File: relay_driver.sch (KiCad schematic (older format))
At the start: 5 parts

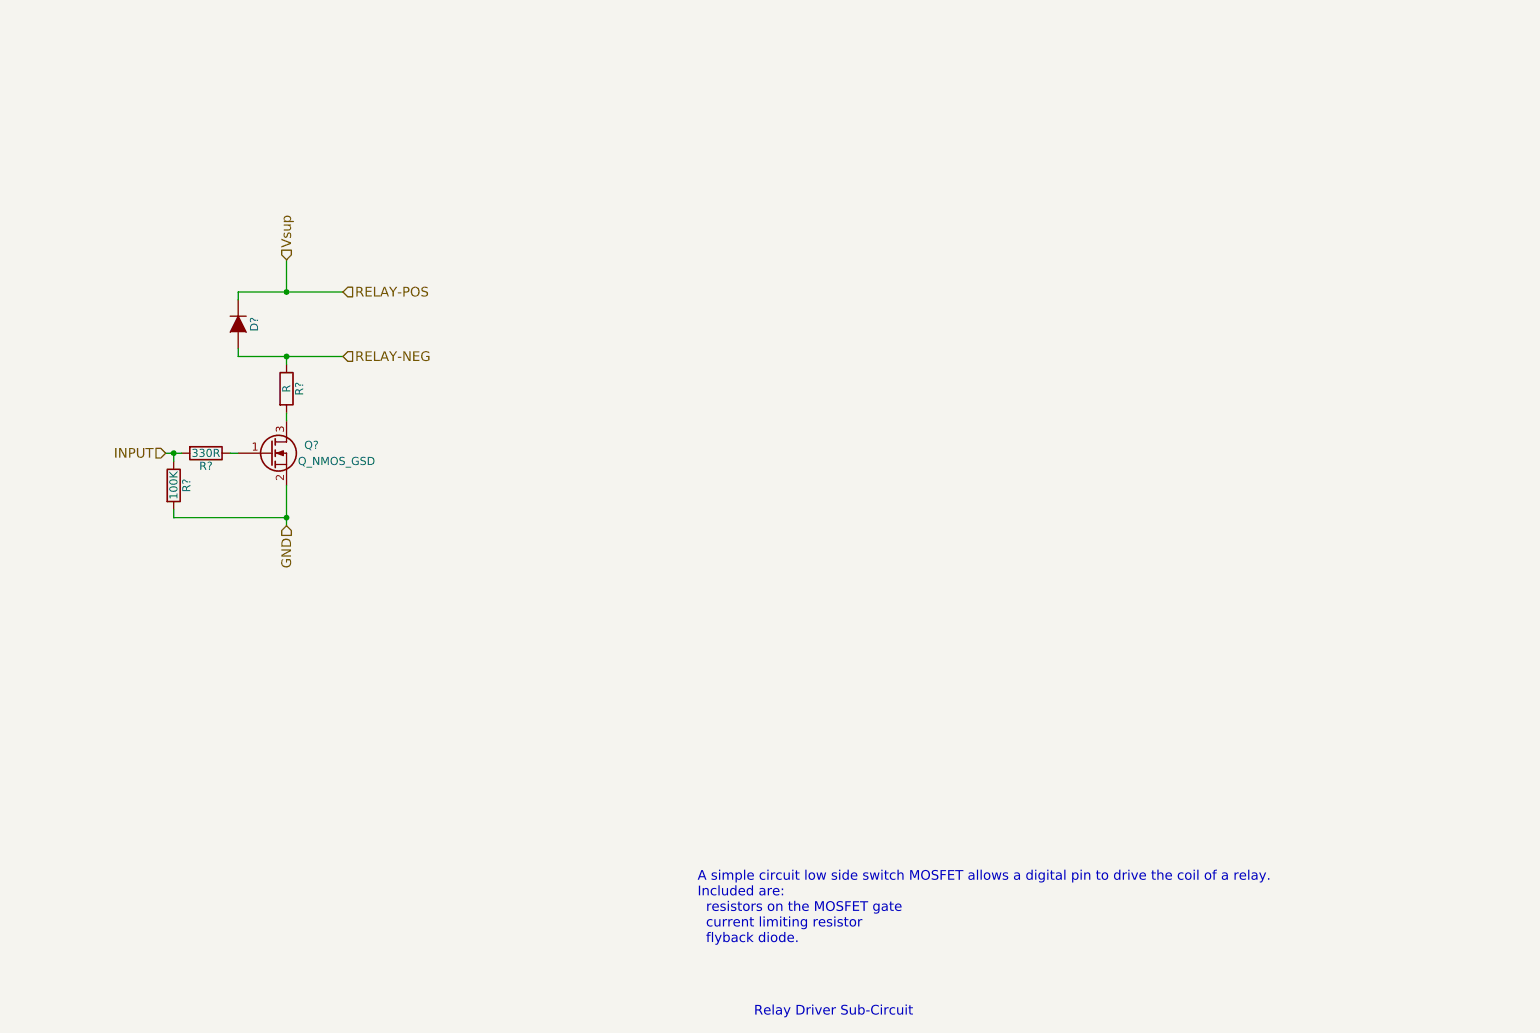
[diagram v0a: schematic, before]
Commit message: added some ICs, started on power, changed sheet sizes
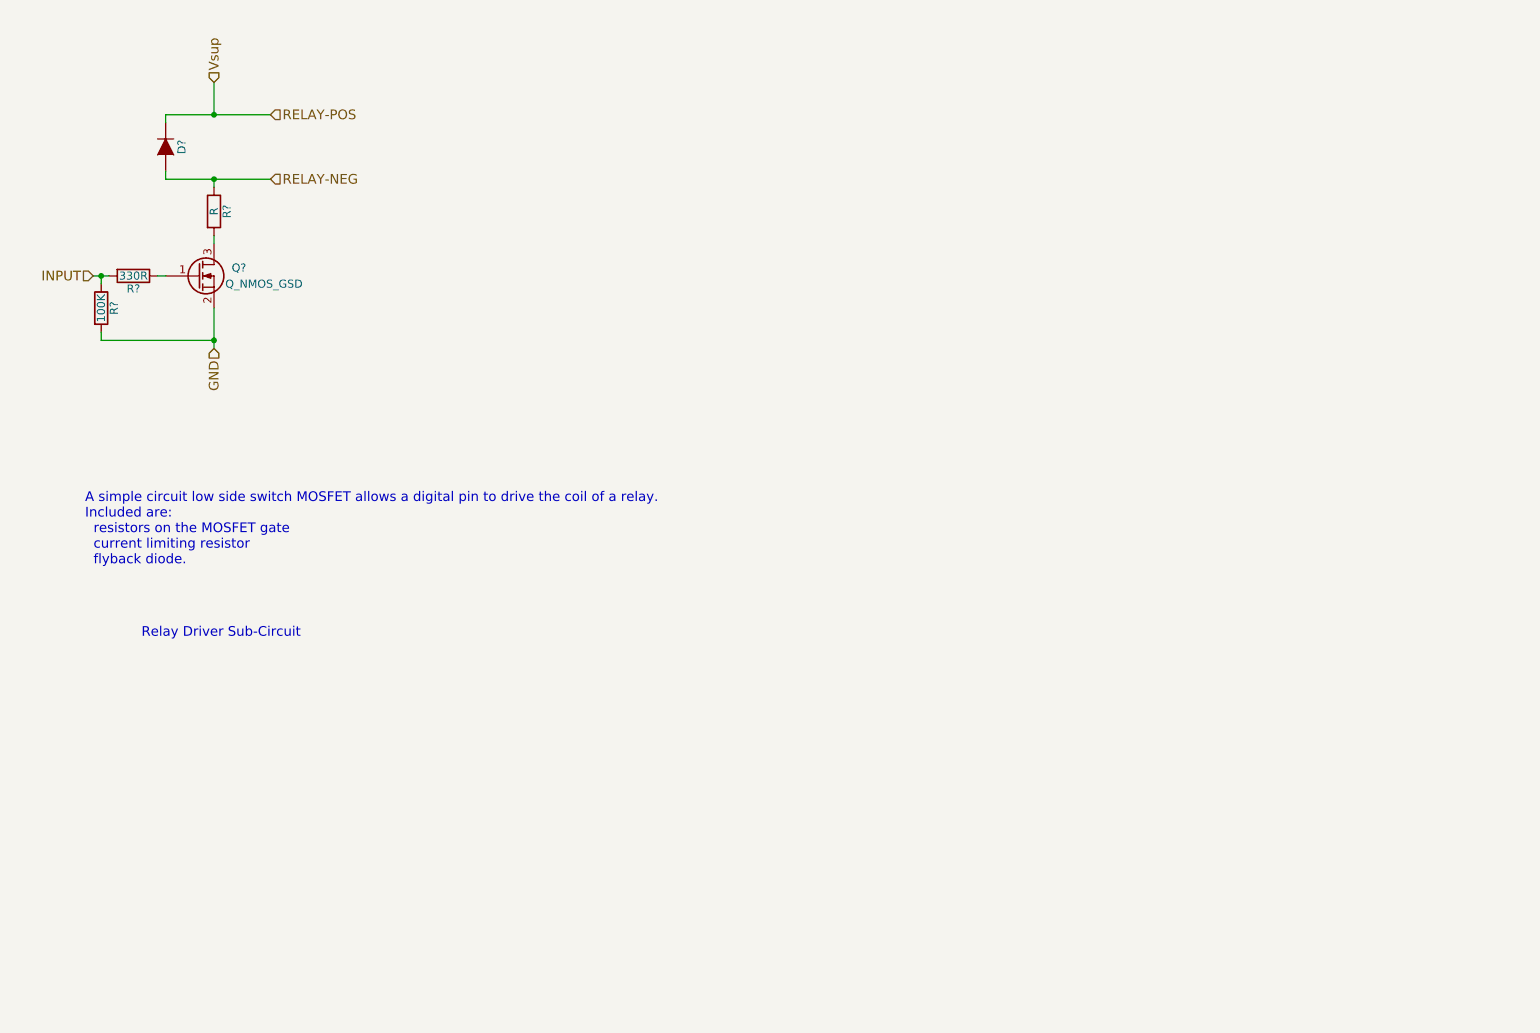
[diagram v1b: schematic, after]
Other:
- moved on the sheet: D?, Q?, R?
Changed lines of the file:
@@
 EELAYER 25 0
 EELAYER END
-$Descr A4 11693 8268
+$Descr User 7874 5906
 encoding utf-8
-Sheet 5 12
+Sheet 2 12
 Title ""
 Date ""
@@
 L Q_NMOS_GSD Q?
 U 1 1 57284B32
-P 4350 4000
+P 3900 2900
 AR Path="/572843F5/57284B32" Ref="Q?"  Part="1"
 AR Path="/5728BD9D/57284B32" Ref="Q?"  Part="1"
-F 0 "Q?" H 4650 4050 50  0000 R CNN
-F 1 "Q_NMOS_GSD" H 5000 3950 50  0000 R CNN
-F 2 "" H 4550 4100 50  0000 C CNN
-F 3 "" H 4350 4000 50  0000 C CNN
-	1    4350 4000
+F 0 "Q?" H 4200 2950 50  0000 R CNN
+F 1 "Q_NMOS_GSD" H 4550 2850 50  0000 R CNN
+F 2 "" H 4100 3000 50  0000 C CNN
+F 3 "" H 3900 2900 50  0000 C CNN
+	1    3900 2900
 	1    0    0    -1
 $EndComp
@@
 L R R?
 U 1 1 57284C7E
-P 3750 4200
+P 3300 3100
 AR Path="/572843F5/57284C7E" Ref="R?"  Part="1"
 AR Path="/5728BD9D/57284C7E" Ref="R?"  Part="1"
-F 0 "R?" V 3830 4200 50  0000 C CNN
-F 1 "100K" V 3750 4200 50  0000 C CNN
-F 2 "" V 3680 4200 50  0000 C CNN
-F 3 "" H 3750 4200 50  0000 C CNN
-	1    3750 4200
+F 0 "R?" V 3380 3100 50  0000 C CNN
+F 1 "100K" V 3300 3100 50  0000 C CNN
+F 2 "" V 3230 3100 50  0000 C CNN
+F 3 "" H 3300 3100 50  0000 C CNN
+	1    3300 3100
 	1    0    0    -1
 $EndComp
@@
 L R R?
 U 1 1 57284CE3
-P 3950 4000
+P 3500 2900
 AR Path="/572843F5/57284CE3" Ref="R?"  Part="1"
 AR Path="/5728BD9D/57284CE3" Ref="R?"  Part="1"
-F 0 "R?" V 4030 4000 50  0000 C CNN
-F 1 "330R" V 3950 4000 50  0000 C CNN
-F 2 "" V 3880 4000 50  0000 C CNN
-F 3 "" H 3950 4000 50  0000 C CNN
-	1    3950 4000
+F 0 "R?" V 3580 2900 50  0000 C CNN
+F 1 "330R" V 3500 2900 50  0000 C CNN
+F 2 "" V 3430 2900 50  0000 C CNN
+F 3 "" H 3500 2900 50  0000 C CNN
+	1    3500 2900
 	0    1    1    0
 $EndComp
@@
 L D D?
 U 1 1 5728508D
-P 4150 3200
+P 3700 2100
 AR Path="/572843F5/5728508D" Ref="D?"  Part="1"
 AR Path="/5728BD9D/5728508D" Ref="D?"  Part="1"
-F 0 "D?" H 4150 3300 50  0000 C CNN
-F 1 "D" H 4150 3100 50  0001 C CNN
-F 2 "" H 4150 3200 50  0000 C CNN
-F 3 "" H 4150 3200 50  0000 C CNN
-	1    4150 3200
+F 0 "D?" H 3700 2200 50  0000 C CNN
+F 1 "D" H 3700 2000 50  0001 C CNN
+F 2 "" H 3700 2100 50  0000 C CNN
+F 3 "" H 3700 2100 50  0000 C CNN
+	1    3700 2100
 	0    1    1    0
 $EndComp
 Wire Wire Line
-	4150 3400 4800 3400
+	3700 2300 4350 2300
 Wire Wire Line
-	4150 3400 4150 3350
-Connection ~ 4450 3400
+	3700 2300 3700 2250
+Connection ~ 4000 2300
 Wire Wire Line
-	4150 3050 4150 3000
+	3700 1950 3700 1900
 $Comp
 L R R?
 U 1 1 5728580D
-P 4450 3600
+P 4000 2500
 AR Path="/572843F5/5728580D" Ref="R?"  Part="1"
 AR Path="/5728BD9D/5728580D" Ref="R?"  Part="1"
-F 0 "R?" V 4530 3600 50  0000 C CNN
-F 1 "R" V 4450 3600 50  0000 C CNN
-F 2 "" V 4380 3600 50  0000 C CNN
-F 3 "" H 4450 3600 50  0000 C CNN
-	1    4450 3600
+F 0 "R?" V 4080 2500 50  0000 C CNN
+F 1 "R" V 4000 2500 50  0000 C CNN
+F 2 "" V 3930 2500 50  0000 C CNN
+F 3 "" H 4000 2500 50  0000 C CNN
+	1    4000 2500
 	1    0    0    -1
 $EndComp
 Wire Wire Line
-	4450 3800 4450 3750
-Text Notes 7350 7500 0    60   ~ 0
+	4000 2700 4000 2650
+Text Notes 3550 5150 0    60   ~ 0
 Relay Driver Sub-Circuit
-Text Notes 7000 7050 0    60   ~ 0
+Text Notes 3200 4700 0    60   ~ 0
 A simple circuit low side switch MOSFET allows a digital pin to drive the coil of a relay.\nIncluded are:\n  resistors on the MOSFET gate\n  current limiting resistor\n  flyback diode.
 Wire Wire Line
-	4450 4200 4450 4450
+	4000 3100 4000 3350
 Wire Wire Line
-	4450 4400 3750 4400
+	4000 3300 3300 3300
 Wire Wire Line
-	3750 4400 3750 4350
+	3300 3300 3300 3250
 Wire Wire Line
-	4100 4000 4150 4000
+	3650 2900 3700 2900
 Wire Wire Line
-	3700 4000 3800 4000
+	3250 2900 3350 2900
 Wire Wire Line
-	3750 4000 3750 4050
+	3300 2900 3300 2950
 Wire Wire Line
-	4450 3450 4450 3400
-Connection ~ 4450 4400
-Text HLabel 4450 4450 3    60   Input ~ 0
+	4000 2350 4000 2300
+Connection ~ 4000 3300
+Text HLabel 4000 3350 3    60   Input ~ 0
 GND
-Connection ~ 3750 4000
-Text HLabel 3700 4000 0    60   Input ~ 0
+Connection ~ 3300 2900
+Text HLabel 3250 2900 0    60   Input ~ 0
 INPUT
-Text HLabel 4450 2800 1    60   Input ~ 0
+Text HLabel 4000 1700 1    60   Input ~ 0
 Vsup
-Text HLabel 4800 3000 2    60   Input ~ 0
+Text HLabel 4350 1900 2    60   Input ~ 0
 RELAY-POS
-Text HLabel 4800 3400 2    60   Input ~ 0
+Text HLabel 4350 2300 2    60   Input ~ 0
 RELAY-NEG
 Wire Wire Line
-	4150 3000 4800 3000
+	3700 1900 4350 1900
 Wire Wire Line
-	4450 2800 4450 3000
-Connection ~ 4450 3000
+	4000 1700 4000 1900
+Connection ~ 4000 1900
 $EndSCHEMATC

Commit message: near done, TODO needs 5V sup from HV, etc
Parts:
- R?: footprint (none) -> Resistors_SMD:R_1206_HandSoldering
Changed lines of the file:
@@
 $Descr User 7874 5906
 encoding utf-8
-Sheet 2 12
+Sheet 4 5
 Title ""
 Date ""
@@
 AR Path="/572843F5/57284B32" Ref="Q?"  Part="1"
 AR Path="/5728BD9D/57284B32" Ref="Q?"  Part="1"
+AR Path="/5728B2EB/57284B32" Ref="Q?"  Part="1"
+AR Path="/5728BD96/57284B32" Ref="Q?"  Part="1"
 F 0 "Q?" H 4200 2950 50  0000 R CNN
 F 1 "Q_NMOS_GSD" H 4550 2850 50  0000 R CNN
@@
 AR Path="/572843F5/57284C7E" Ref="R?"  Part="1"
 AR Path="/5728BD9D/57284C7E" Ref="R?"  Part="1"
+AR Path="/5728B2EB/57284C7E" Ref="R?"  Part="1"
+AR Path="/5728BD96/57284C7E" Ref="R?"  Part="1"
 F 0 "R?" V 3380 3100 50  0000 C CNN
 F 1 "100K" V 3300 3100 50  0000 C CNN
@@
 AR Path="/572843F5/57284CE3" Ref="R?"  Part="1"
 AR Path="/5728BD9D/57284CE3" Ref="R?"  Part="1"
+AR Path="/5728B2EB/57284CE3" Ref="R?"  Part="1"
+AR Path="/5728BD96/57284CE3" Ref="R?"  Part="1"
 F 0 "R?" V 3580 2900 50  0000 C CNN
 F 1 "330R" V 3500 2900 50  0000 C CNN
@@
 AR Path="/572843F5/5728508D" Ref="D?"  Part="1"
 AR Path="/5728BD9D/5728508D" Ref="D?"  Part="1"
+AR Path="/5728B2EB/5728508D" Ref="D?"  Part="1"
+AR Path="/5728BD96/5728508D" Ref="D?"  Part="1"
 F 0 "D?" H 3700 2200 50  0000 C CNN
 F 1 "D" H 3700 2000 50  0001 C CNN
@@
 AR Path="/572843F5/5728580D" Ref="R?"  Part="1"
 AR Path="/5728BD9D/5728580D" Ref="R?"  Part="1"
+AR Path="/5728B2EB/5728580D" Ref="R?"  Part="1"
+AR Path="/5728BD96/5728580D" Ref="R?"  Part="1"
 F 0 "R?" V 4080 2500 50  0000 C CNN
-F 1 "R" V 4000 2500 50  0000 C CNN
-F 2 "" V 3930 2500 50  0000 C CNN
+F 1 "R" V 4000 2500 50  0001 C CNN
+F 2 "Resistors_SMD:R_1206_HandSoldering" V 3930 2500 50  0001 C CNN
 F 3 "" H 4000 2500 50  0000 C CNN
 	1    4000 2500

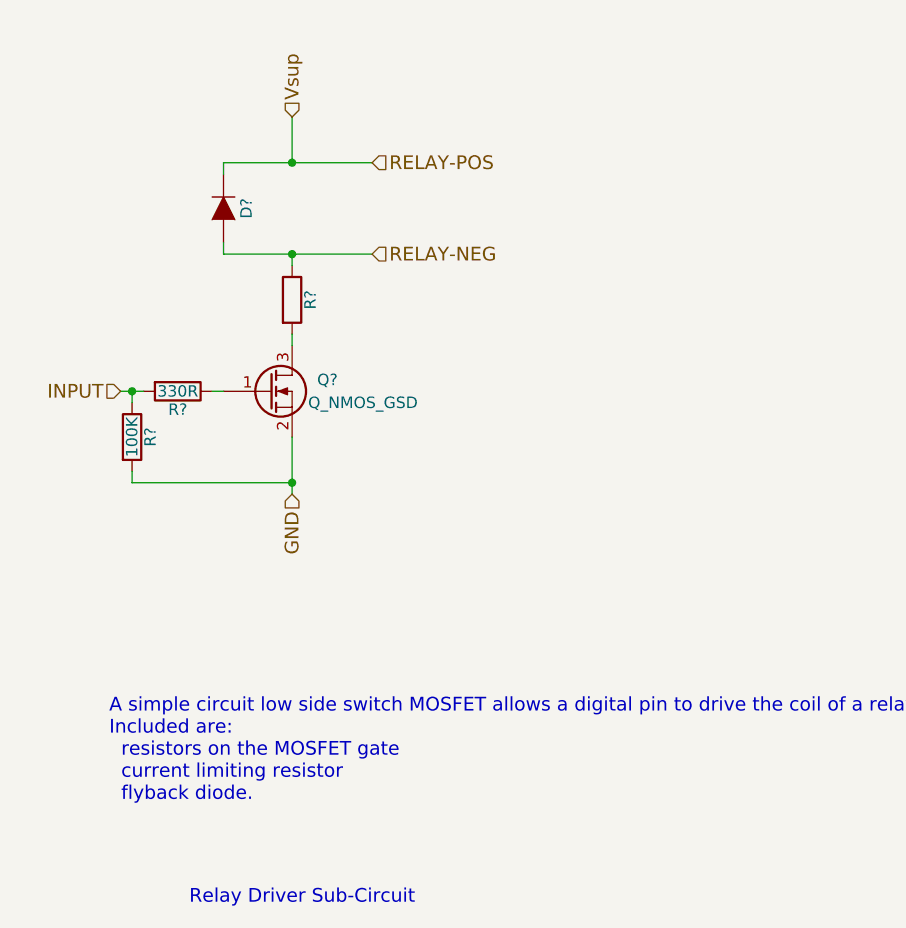
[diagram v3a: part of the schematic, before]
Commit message: WIP but mostly done, needs connector
latch switch changed to using photorelays
added watchdog to relays
added two unidirectional precharge subcircuits
moved ILV relay to onboard
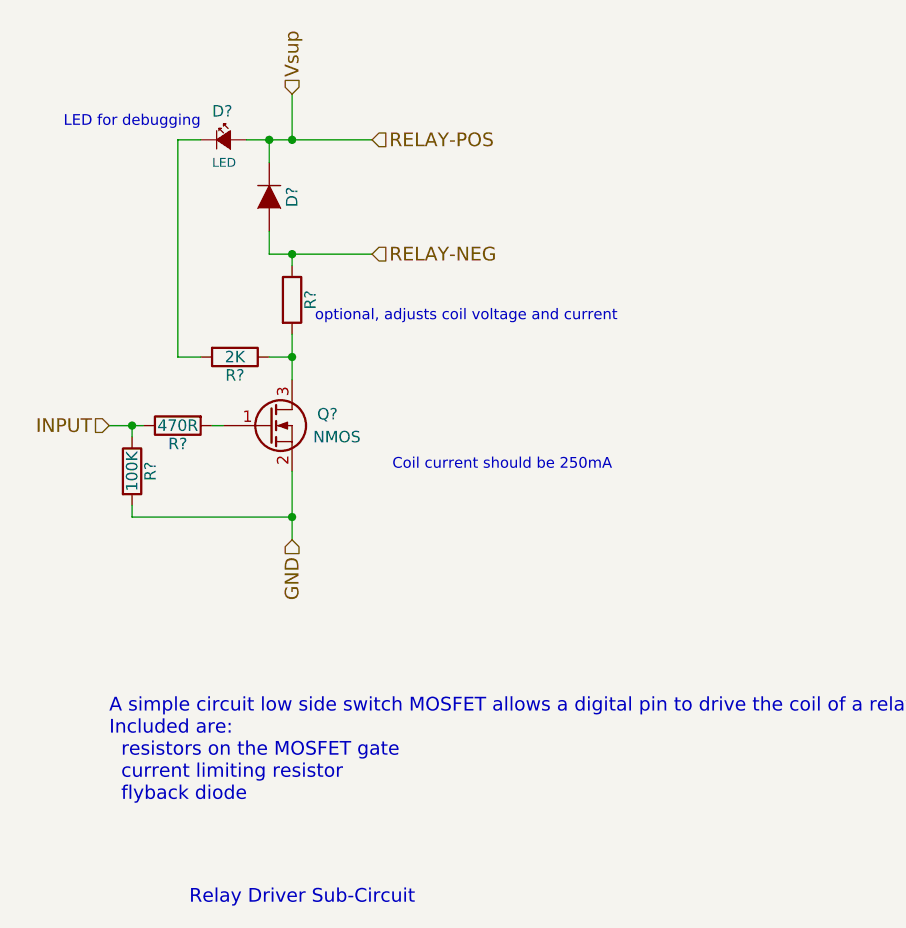
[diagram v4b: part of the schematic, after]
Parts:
- added D?: LED, symbol Led_Small
- added R?: 2K, Resistors_SMD:R_1206_HandSoldering, symbol R
- Q?: value Q_NMOS_GSD -> NMOS
- R?: value 330R -> 470R
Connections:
- net INPUT: now also R?.1; no longer R?.2
- net RELAY-POS: now also D?.2 (A)
- net at Q?.1 (G): now also R?.2; no longer R?.1
- net at Q?.3 (D), R?.2: now also R?.1
- new net: D?.1 (K), R?.2
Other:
- note added: "A simple circuit low side switch MOSFET allows a digital pin to drive the coil of a relay.\nIncluded are:\n resistors on the MOSFET gate\n current limiting resistor\n flyback diode"
- note added: "Coil current should be 250mA"
- note added: "LED for debugging"
- note added: "optional, adjusts coil voltage and current"
- note removed: "A simple circuit low side switch MOSFET allows a digital pin to drive the coil of a relay.\nIncluded are:\n resistors on the MOSFET gate\n current limiting resistor\n flyback diode."
- moved on the sheet: D?, Q?, R?
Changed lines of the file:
@@
 $Descr User 7874 5906
 encoding utf-8
-Sheet 4 7
+Sheet 2 5
 Title ""
 Date ""
@@
 L Q_NMOS_GSD Q?
 U 1 1 57284B32
-P 3900 2900
+P 3900 3050
 AR Path="/572843F5/57284B32" Ref="Q?"  Part="1"
 AR Path="/5728BD9D/57284B32" Ref="Q?"  Part="1"
 AR Path="/5728B2EB/57284B32" Ref="Q?"  Part="1"
 AR Path="/5728BD96/57284B32" Ref="Q?"  Part="1"
-F 0 "Q?" H 4200 2950 50  0000 R CNN
-F 1 "Q_NMOS_GSD" H 4550 2850 50  0000 R CNN
-F 2 "" H 4100 3000 50  0000 C CNN
-F 3 "" H 3900 2900 50  0000 C CNN
-	1    3900 2900
+F 0 "Q?" H 4200 3100 50  0000 R CNN
+F 1 "NMOS" H 4300 3000 50  0000 R CNN
+F 2 "" H 4100 3150 50  0000 C CNN
+F 3 "" H 3900 3050 50  0000 C CNN
+	1    3900 3050
 	1    0    0    -1
 $EndComp
@@
 L R R?
 U 1 1 57284C7E
-P 3300 3100
+P 3300 3250
 AR Path="/572843F5/57284C7E" Ref="R?"  Part="1"
 AR Path="/5728BD9D/57284C7E" Ref="R?"  Part="1"
 AR Path="/5728B2EB/57284C7E" Ref="R?"  Part="1"
 AR Path="/5728BD96/57284C7E" Ref="R?"  Part="1"
-F 0 "R?" V 3380 3100 50  0000 C CNN
-F 1 "100K" V 3300 3100 50  0000 C CNN
-F 2 "" V 3230 3100 50  0000 C CNN
-F 3 "" H 3300 3100 50  0000 C CNN
-	1    3300 3100
+F 0 "R?" V 3380 3250 50  0000 C CNN
+F 1 "100K" V 3300 3250 50  0000 C CNN
+F 2 "" V 3230 3250 50  0000 C CNN
+F 3 "" H 3300 3250 50  0000 C CNN
+	1    3300 3250
 	1    0    0    -1
 $EndComp
@@
 L R R?
 U 1 1 57284CE3
-P 3500 2900
+P 3500 3050
 AR Path="/572843F5/57284CE3" Ref="R?"  Part="1"
 AR Path="/5728BD9D/57284CE3" Ref="R?"  Part="1"
 AR Path="/5728B2EB/57284CE3" Ref="R?"  Part="1"
 AR Path="/5728BD96/57284CE3" Ref="R?"  Part="1"
-F 0 "R?" V 3580 2900 50  0000 C CNN
-F 1 "330R" V 3500 2900 50  0000 C CNN
-F 2 "" V 3430 2900 50  0000 C CNN
-F 3 "" H 3500 2900 50  0000 C CNN
-	1    3500 2900
-	0    1    1    0
+F 0 "R?" V 3580 3050 50  0000 C CNN
+F 1 "470R" V 3500 3050 50  0000 C CNN
+F 2 "" V 3430 3050 50  0000 C CNN
+F 3 "" H 3500 3050 50  0000 C CNN
+	1    3500 3050
+	0    -1   1    0
 $EndComp
 $Comp
 L D D?
 U 1 1 5728508D
-P 3700 2100
+P 3900 2050
 AR Path="/572843F5/5728508D" Ref="D?"  Part="1"
 AR Path="/5728BD9D/5728508D" Ref="D?"  Part="1"
 AR Path="/5728B2EB/5728508D" Ref="D?"  Part="1"
 AR Path="/5728BD96/5728508D" Ref="D?"  Part="1"
-F 0 "D?" H 3700 2200 50  0000 C CNN
-F 1 "D" H 3700 2000 50  0001 C CNN
-F 2 "" H 3700 2100 50  0000 C CNN
-F 3 "" H 3700 2100 50  0000 C CNN
-	1    3700 2100
+F 0 "D?" H 3900 2150 50  0000 C CNN
+F 1 "D" H 3900 1950 50  0001 C CNN
+F 2 "" H 3900 2050 50  0000 C CNN
+F 3 "" H 3900 2050 50  0000 C CNN
+	1    3900 2050
 	0    1    1    0
 $EndComp
 Wire Wire Line
-	3700 2300 4350 2300
+	3900 2300 4000 2300
 Wire Wire Line
-	3700 2300 3700 2250
+	4000 2300 4350 2300
+Wire Wire Line
+	3900 2300 3900 2200
 Connection ~ 4000 2300
 Wire Wire Line
-	3700 1950 3700 1900
+	3900 1900 3900 1800
 $Comp
 L R R?
@@
 $EndComp
 Wire Wire Line
-	4000 2700 4000 2650
+	4000 2850 4000 2750
+Wire Wire Line
+	4000 2750 4000 2650
 Text Notes 3550 5150 0    60   ~ 0
 Relay Driver Sub-Circuit
 Text Notes 3200 4700 0    60   ~ 0
-A simple circuit low side switch MOSFET allows a digital pin to drive the coil of a relay.\nIncluded are:\n  resistors on the MOSFET gate\n  current limiting resistor\n  flyback diode.
+A simple circuit low side switch MOSFET allows a digital pin to drive the coil of a relay.\nIncluded are:\n  resistors on the MOSFET gate\n  current limiting resistor\n  flyback diode
 Wire Wire Line
-	4000 3100 4000 3350
+	4000 3250 4000 3450
 Wire Wire Line
-	4000 3300 3300 3300
+	4000 3450 4000 3550
 Wire Wire Line
-	3300 3300 3300 3250
+	4000 3450 3300 3450
 Wire Wire Line
-	3650 2900 3700 2900
+	3300 3450 3300 3400
 Wire Wire Line
-	3250 2900 3350 2900
+	3650 3050 3700 3050
 Wire Wire Line
-	3300 2900 3300 2950
+	3200 3050 3300 3050
+Wire Wire Line
+	3300 3050 3350 3050
+Wire Wire Line
+	3300 3050 3300 3100
 Wire Wire Line
 	4000 2350 4000 2300
-Connection ~ 4000 3300
-Text HLabel 4000 3350 3    60   Input ~ 0
+Connection ~ 4000 3450
+Text HLabel 4000 3550 3    60   Input ~ 0
 GND
-Connection ~ 3300 2900
-Text HLabel 3250 2900 0    60   Input ~ 0
+Connection ~ 3300 3050
+Text HLabel 3200 3050 0    60   Input ~ 0
 INPUT
-Text HLabel 4000 1700 1    60   Input ~ 0
+Text HLabel 4000 1600 1    60   Input ~ 0
 Vsup
-Text HLabel 4350 1900 2    60   Input ~ 0
+Text HLabel 4350 1800 2    60   Input ~ 0
 RELAY-POS
 Text HLabel 4350 2300 2    60   Input ~ 0
 RELAY-NEG
 Wire Wire Line
-	3700 1900 4350 1900
+	3800 1800 3900 1800
 Wire Wire Line
-	4000 1700 4000 1900
-Connection ~ 4000 1900
+	3900 1800 4000 1800
+Wire Wire Line
+	4000 1800 4350 1800
+Wire Wire Line
+	4000 1600 4000 1800
+Connection ~ 4000 1800
+$Comp
+L Led_Small D?
+U 1 1 573F0404
+P 3700 1800
+F 0 "D?" H 3650 1925 50  0000 L CNN
+F 1 "LED" H 3650 1700 39  0000 L CNN
+F 2 "" V 3700 1800 50  0000 C CNN
+F 3 "" V 3700 1800 50  0000 C CNN
+	1    3700 1800
+	1    0    0    -1
+$EndComp
+$Comp
+L R R?
+U 1 1 573F0488
+P 3750 2750
+F 0 "R?" V 3830 2750 50  0000 C CNN
+F 1 "2K" V 3750 2750 50  0000 C CNN
+F 2 "Resistors_SMD:R_1206_HandSoldering" V 3680 2750 50  0001 C CNN
+F 3 "" H 3750 2750 50  0000 C CNN
+	1    3750 2750
+	0    1    1    0
+$EndComp
+Wire Wire Line
+	3600 2750 3500 2750
+Wire Wire Line
+	3500 2750 3500 1800
+Wire Wire Line
+	3500 1800 3600 1800
+Connection ~ 3900 1800
+Wire Wire Line
+	3900 2750 4000 2750
+Connection ~ 4000 2750
+Text Notes 4100 2600 0    47   ~ 0
+optional, adjusts coil voltage and current
+Text Notes 3600 1750 2    47   ~ 0
+LED for debugging
+Text Notes 5400 3250 2    47   ~ 0
+Coil current should be 250mA
 $EndSCHEMATC
